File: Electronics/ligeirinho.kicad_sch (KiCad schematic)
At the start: 28 parts, among them J1 Bateria, J10 ponte H ld ESP, J11 VS1838B, J12 MPU6050, J13 ADNS-9500, J14 ADNS-9500 3V3, J2 ESP32 esq, J3 ESP32 dir, J4 VL53L0X 1, J5 VL53L0X 2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

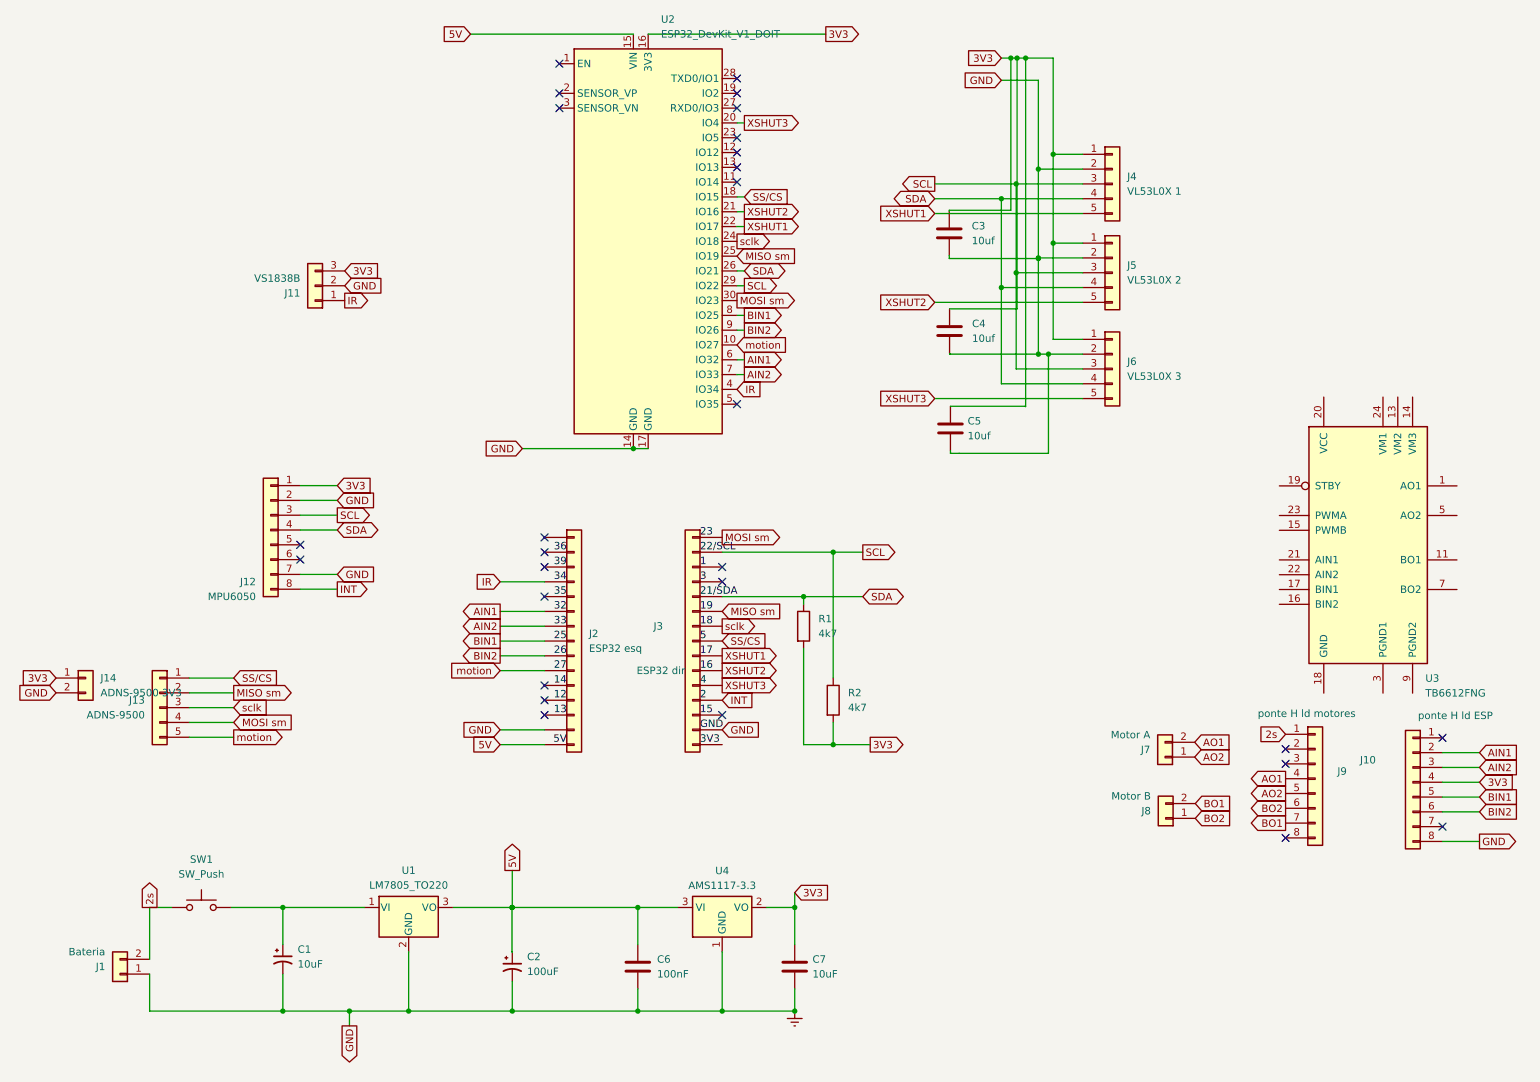
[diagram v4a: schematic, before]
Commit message: chore: add mouse sensor to pcb and fix some measures
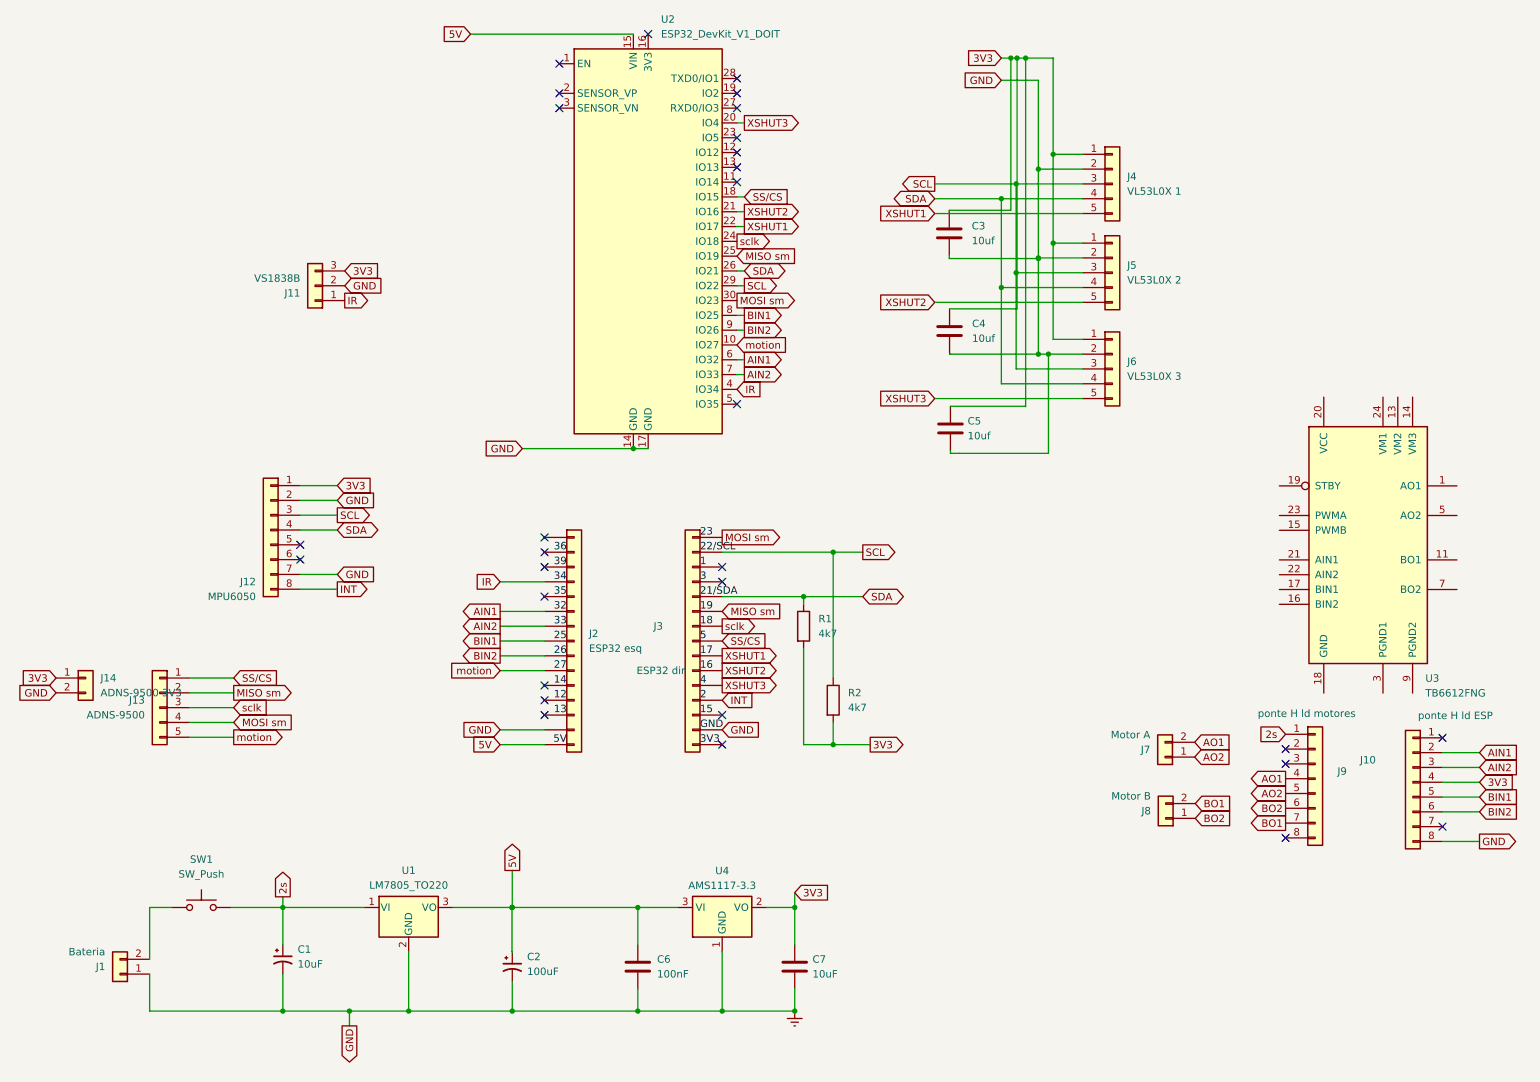
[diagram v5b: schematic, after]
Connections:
- net 2s: now also C1.1, SW1.2, U1.1 (VI); no longer J1.2 (Pin_2), SW1.1
- net 3V3: no longer U2.16 (3V3)
- new net: J1.2 (Pin_2), SW1.1
- no-connect marks 28 -> 30
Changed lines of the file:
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@@
   (junction (at 188.0616 68.8848) (diameter 0) (color 0 0 0 0)
   )
+  (junction (at 186.3344 37.1348) (diameter 0) (color 0 0 0 1)
+  )
+  (junction (at 186.3344 52.3748) (diameter 0) (color 0 0 0 1)
+  )
+  (junction (at 184.15 18.0848) (diameter 0) (color 0 0 0 0)
+  )
+  (junction (at 78.2828 181.61) (diameter 0) (color 0 0 0 0)
+  )
+  (junction (at 151.13 135.89) (diameter 0) (color 0 0 0 0)
+  )
+  (junction (at 56.6928 181.61) (diameter 0) (color 0 0 0 0)
+  )
+  (junction (at 96.0628 163.83) (diameter 0) (color 0 0 0 0)
+  )
+  (junction (at 144.526 163.83) (diameter 0) (color 0 0 0 0)
+  )
+  (junction (at 182.5244 54.9148) (diameter 0) (color 0 0 0 0)
+  )
+  (junction (at 179.9844 42.2148) (diameter 0) (color 0 0 0 0)
+  )
+  (junction (at 117.602 181.61) (diameter 0) (color 0 0 0 0)
+  )
+  (junction (at 151.13 102.87) (diameter 0) (color 0 0 0 0)
+  )
+  (junction (at 186.3344 68.8848) (diameter 0) (color 0 0 0 0)
+  )
   (junction (at 56.6928 163.83) (diameter 0) (color 0 0 0 0)
-  )
-  (junction (at 186.3344 37.1348) (diameter 0) (color 0 0 0 1)
-  )
-  (junction (at 186.3344 52.3748) (diameter 0) (color 0 0 0 1)
-  )
-  (junction (at 184.15 18.0848) (diameter 0) (color 0 0 0 0)
-  )
-  (junction (at 78.2828 181.61) (diameter 0) (color 0 0 0 0)
-  )
-  (junction (at 151.13 135.89) (diameter 0) (color 0 0 0 0)
-  )
-  (junction (at 56.6928 181.61) (diameter 0) (color 0 0 0 0)
-  )
-  (junction (at 96.0628 163.83) (diameter 0) (color 0 0 0 0)
-  )
-  (junction (at 144.526 163.83) (diameter 0) (color 0 0 0 0)
-  )
-  (junction (at 182.5244 54.9148) (diameter 0) (color 0 0 0 0)
-  )
-  (junction (at 179.9844 42.2148) (diameter 0) (color 0 0 0 0)
-  )
-  (junction (at 117.602 181.61) (diameter 0) (color 0 0 0 0)
-  )
-  (junction (at 151.13 102.87) (diameter 0) (color 0 0 0 0)
-  )
-  (junction (at 186.3344 68.8848) (diameter 0) (color 0 0 0 0)
   )
   (junction (at 146.05 110.49) (diameter 0) (color 0 0 0 0)
@@
   (no_connect (at 104.14 24.13))
   (no_connect (at 132.08 130.81))
+  (no_connect (at 132.08 135.89))
   (no_connect (at 104.14 26.67))
   (no_connect (at 228.7524 136.652))
+  (no_connect (at 119.38 13.97))
   (no_connect (at 101.6 128.27))
   (no_connect (at 101.6 100.33))
@@
     (stroke (width 0) (type default))
   )
+  (wire (pts (xy 56.6928 163.83) (xy 70.6628 163.83))
+    (stroke (width 0) (type default))
+  )
   (wire (pts (xy 96.012 163.83) (xy 96.012 171.45))
     (stroke (width 0) (type default))
@@
     (stroke (width 0) (type default))
   )
+  (wire (pts (xy 33.8328 172.72) (xy 33.8328 163.83))
+    (stroke (width 0) (type default))
+  )
   (wire (pts (xy 97.79 85.09) (xy 116.84 85.09))
     (stroke (width 0) (type default))
@@
     (stroke (width 0) (type default))
   )
-  (wire (pts (xy 33.8328 163.83) (xy 33.8328 172.72))
-    (stroke (width 0) (type default))
-  )
   (wire (pts (xy 88.9 13.97) (xy 116.84 13.97))
     (stroke (width 0) (type default))
@@
     (stroke (width 0) (type default))
   )
-  (wire (pts (xy 56.6928 163.83) (xy 70.6628 163.83))
+  (wire (pts (xy 47.8028 163.83) (xy 56.6928 163.83))
     (stroke (width 0) (type default))
   )
@@
     (stroke (width 0) (type default))
   )
-  (wire (pts (xy 119.38 13.97) (xy 149.86 13.97))
-    (stroke (width 0) (type default))
-  )
   (wire (pts (xy 184.0992 77.8764) (xy 184.0992 77.8256))
     (stroke (width 0) (type default))
   )
+  (wire (pts (xy 255.6764 137.2616) (xy 262.0264 137.2616))
+    (stroke (width 0) (type default))
+  )
+  (wire (pts (xy 134.62 54.61) (xy 135.89 54.61))
+    (stroke (width 0) (type default))
+  )
+  (wire (pts (xy 40.64 129.54) (xy 48.26 129.54))
+    (stroke (width 0) (type default))
+  )
+  (wire (pts (xy 168.5544 76.5048) (xy 193.9544 76.5048))
+    (stroke (width 0) (type default))
+  )
+  (wire (pts (xy 93.98 118.11) (xy 101.6 118.11))
+    (stroke (width 0) (type default))
+  )
+  (wire (pts (xy 151.13 102.87) (xy 151.13 124.46))
+    (stroke (width 0) (type default))
+  )
+  (wire (pts (xy 255.6764 139.8016) (xy 262.0264 139.8016))
+    (stroke (width 0) (type default))
+  )
+  (wire (pts (xy 184.0992 77.8256) (xy 171.2468 77.8256))
+    (stroke (width 0) (type default))
+  )
+  (wire (pts (xy 40.64 134.62) (xy 48.26 134.62))
+    (stroke (width 0) (type default))
+  )
+  (wire (pts (xy 40.64 132.08) (xy 48.26 132.08))
+    (stroke (width 0) (type default))
+  )
+  (wire (pts (xy 96.012 171.45) (xy 96.0628 171.45))
+    (stroke (width 0) (type default))
+  )
+  (wire (pts (xy 134.62 57.15) (xy 135.89 57.15))
+    (stroke (width 0) (type default))
+  )
+  (wire (pts (xy 182.5244 54.9148) (xy 193.9544 54.9148))
+    (stroke (width 0) (type default))
+  )
+  (wire (pts (xy 96.0628 176.53) (xy 96.0628 181.61))
+    (stroke (width 0) (type default))
+  )
+  (wire (pts (xy 78.2828 181.61) (xy 78.2828 171.45))
+    (stroke (width 0) (type default))
+  )
+  (wire (pts (xy 188.8744 49.8348) (xy 193.9544 49.8348))
+    (stroke (width 0) (type default))
+  )
+  (wire (pts (xy 144.526 163.83) (xy 144.526 170.18))
+    (stroke (width 0) (type default))
+  )
+  (wire (pts (xy 93.98 120.65) (xy 101.6 120.65))
+    (stroke (width 0) (type default))
+  )
+  (wire (pts (xy 144.526 177.8) (xy 144.526 181.61))
+    (stroke (width 0) (type default))
+  )
+  (wire (pts (xy 186.3344 68.8848) (xy 171.1452 68.8848))
+    (stroke (width 0) (type default) (color 0 0 0 1))
+  )
   (wire (pts (xy 33.8328 163.83) (xy 37.6428 163.83))
     (stroke (width 0) (type default))
   )
-  (wire (pts (xy 255.6764 137.2616) (xy 262.0264 137.2616))
-    (stroke (width 0) (type default))
-  )
-  (wire (pts (xy 134.62 54.61) (xy 135.89 54.61))
-    (stroke (width 0) (type default))
-  )
-  (wire (pts (xy 40.64 129.54) (xy 48.26 129.54))
-    (stroke (width 0) (type default))
-  )
-  (wire (pts (xy 168.5544 76.5048) (xy 193.9544 76.5048))
-    (stroke (width 0) (type default))
-  )
-  (wire (pts (xy 93.98 118.11) (xy 101.6 118.11))
-    (stroke (width 0) (type default))
-  )
-  (wire (pts (xy 151.13 102.87) (xy 151.13 124.46))
-    (stroke (width 0) (type default))
-  )
-  (wire (pts (xy 255.6764 139.8016) (xy 262.0264 139.8016))
-    (stroke (width 0) (type default))
-  )
-  (wire (pts (xy 184.0992 77.8256) (xy 171.2468 77.8256))
-    (stroke (width 0) (type default))
-  )
-  (wire (pts (xy 40.64 134.62) (xy 48.26 134.62))
-    (stroke (width 0) (type default))
-  )
-  (wire (pts (xy 40.64 132.08) (xy 48.26 132.08))
-    (stroke (width 0) (type default))
-  )
-  (wire (pts (xy 96.012 171.45) (xy 96.0628 171.45))
-    (stroke (width 0) (type default))
-  )
-  (wire (pts (xy 134.62 57.15) (xy 135.89 57.15))
-    (stroke (width 0) (type default))
-  )
-  (wire (pts (xy 182.5244 54.9148) (xy 193.9544 54.9148))
-    (stroke (width 0) (type default))
-  )
-  (wire (pts (xy 96.0628 176.53) (xy 96.0628 181.61))
-    (stroke (width 0) (type default))
-  )
-  (wire (pts (xy 78.2828 181.61) (xy 78.2828 171.45))
-    (stroke (width 0) (type default))
-  )
-  (wire (pts (xy 188.8744 49.8348) (xy 193.9544 49.8348))
-    (stroke (width 0) (type default))
-  )
-  (wire (pts (xy 144.526 163.83) (xy 144.526 170.18))
-    (stroke (width 0) (type default))
-  )
-  (wire (pts (xy 93.98 120.65) (xy 101.6 120.65))
-    (stroke (width 0) (type default))
-  )
-  (wire (pts (xy 144.526 177.8) (xy 144.526 181.61))
-    (stroke (width 0) (type default))
-  )
-  (wire (pts (xy 186.3344 68.8848) (xy 171.1452 68.8848))
-    (stroke (width 0) (type default) (color 0 0 0 1))
-  )
   (wire (pts (xy 184.0992 77.8764) (xy 184.15 77.8764))
     (stroke (width 0) (type default))
@@
     (stroke (width 0) (type default))
   )
-  (wire (pts (xy 47.8028 163.83) (xy 56.6928 163.83))
-    (stroke (width 0) (type default))
-  )
   (wire (pts (xy 151.13 102.87) (xy 156.21 102.87))
     (stroke (width 0) (type default))
@@
   (wire (pts (xy 186.3344 68.8848) (xy 188.0616 68.8848))
     (stroke (width 0) (type default) (color 0 0 0 1))
+  )
+  (wire (pts (xy 56.6928 162.0012) (xy 56.6928 163.83))
+    (stroke (width 0) (type default))
   )
   (wire (pts (xy 59.69 96.52) (xy 66.04 96.52))
@@
     )
   )
-  (global_label "3V3" (shape output) (at 149.86 13.97 0) (fields_autoplaced)
-    (effects (font (size 1.27 1.27)) (justify left))
-    (property "Intersheetrefs" "${INTERSHEET_REFS}" (at 156.3528 13.97 0)
-      (effects (font (size 1.27 1.27)) (justify left) hide)
-    )
-  )
   (global_label "MOSI sm" (shape output) (at 134.62 59.69 0) (fields_autoplaced)
     (effects (font (size 1.27 1.27)) (justify left))
@@
     )
   )
-  (global_label "2s" (shape output) (at 33.8328 163.83 90) (fields_autoplaced)
-    (effects (font (size 1.27 1.27)) (justify left))
-    (property "Intersheetrefs" "${INTERSHEET_REFS}" (at 33.8328 158.6072 90)
-      (effects (font (size 1.27 1.27)) (justify left) hide)
-    )
+  (global_label "2s" (shape output) (at 56.6928 162.0012 90) (fields_autoplaced)
+    (effects (font (size 1.27 1.27)) (justify left))
+    (property "Intersheetrefs" "${INTERSHEET_REFS}" (at 56.6928 156.7784 90)
+      (effects (font (size 1.27 1.27)) (justify left) hide)
+    )

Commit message: feat: add autonomous stategy
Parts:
- C3, C4, C5, C6, C7: footprint Capacitor_SMD:C_0805_2012Metric_Pad1.18x1.45mm_HandSolder -> Capacitor_SMD:C_0201_0603Metric
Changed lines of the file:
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@@
       (effects (font (size 1.27 1.27)) (justify left))
     )
-    (property "Footprint" "Capacitor_SMD:C_0805_2012Metric_Pad1.18x1.45mm_HandSolder" (at 145.4912 177.8 0)
+    (property "Footprint" "Capacitor_SMD:C_0201_0603Metric" (at 145.4912 177.8 0)
       (effects (font (size 1.27 1.27)) hide)
     )
@@
       (effects (font (size 1.27 1.27)) (justify left))
     )
-    (property "Footprint" "Capacitor_SMD:C_0805_2012Metric_Pad1.18x1.45mm_HandSolder" (at 118.5672 177.8 0)
+    (property "Footprint" "Capacitor_SMD:C_0201_0603Metric" (at 118.5672 177.8 0)
       (effects (font (size 1.27 1.27)) hide)
     )
@@
       (effects (font (size 1.27 1.27)) (justify left))
     )
-    (property "Footprint" "Capacitor_SMD:C_0805_2012Metric_Pad1.18x1.45mm_HandSolder" (at 172.0088 51.9684 0)
+    (property "Footprint" "Capacitor_SMD:C_0201_0603Metric" (at 172.0088 51.9684 0)
       (effects (font (size 1.27 1.27)) hide)
     )
@@
       (effects (font (size 1.27 1.27)) (justify left))
     )
-    (property "Footprint" "Capacitor_SMD:C_0805_2012Metric_Pad1.18x1.45mm_HandSolder" (at 172.0596 68.7324 0)
+    (property "Footprint" "Capacitor_SMD:C_0201_0603Metric" (at 172.0596 68.7324 0)
       (effects (font (size 1.27 1.27)) hide)
     )
@@
       (effects (font (size 1.27 1.27)) (justify left))
     )
-    (property "Footprint" "Capacitor_SMD:C_0805_2012Metric_Pad1.18x1.45mm_HandSolder" (at 172.212 85.4456 0)
-      (effects (font (size 1.27 1.27)) hide)
-    )
+    (property "Footprint" "Capacitor_SMD:C_0201_0603Metric" (at 172.212 85.4456 0)
+      (effects (font (size 1.27 1.27)) hide)
+    )
